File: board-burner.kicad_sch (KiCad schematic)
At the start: 44 parts, among them J1 Conn_01x04_Socket, J2 TH1, J3 FAN, J4 HEATER, J5 AUX2, J6 Micro_SD_Card, J7 AUX1, J8 TH2, J9 MAINS, Q1 2N7000, Q2 Q_NMOS_DGS, Q3 Q_PMOS_DGS, Q4 Q_NMOS_DGS, Q5 Q_NMOS_DGS, Q6 Q_NMOS_DGS, SW1 PWR, U1 10A SSR, U2 MAX31855KASA, U4 MAX31855KASA

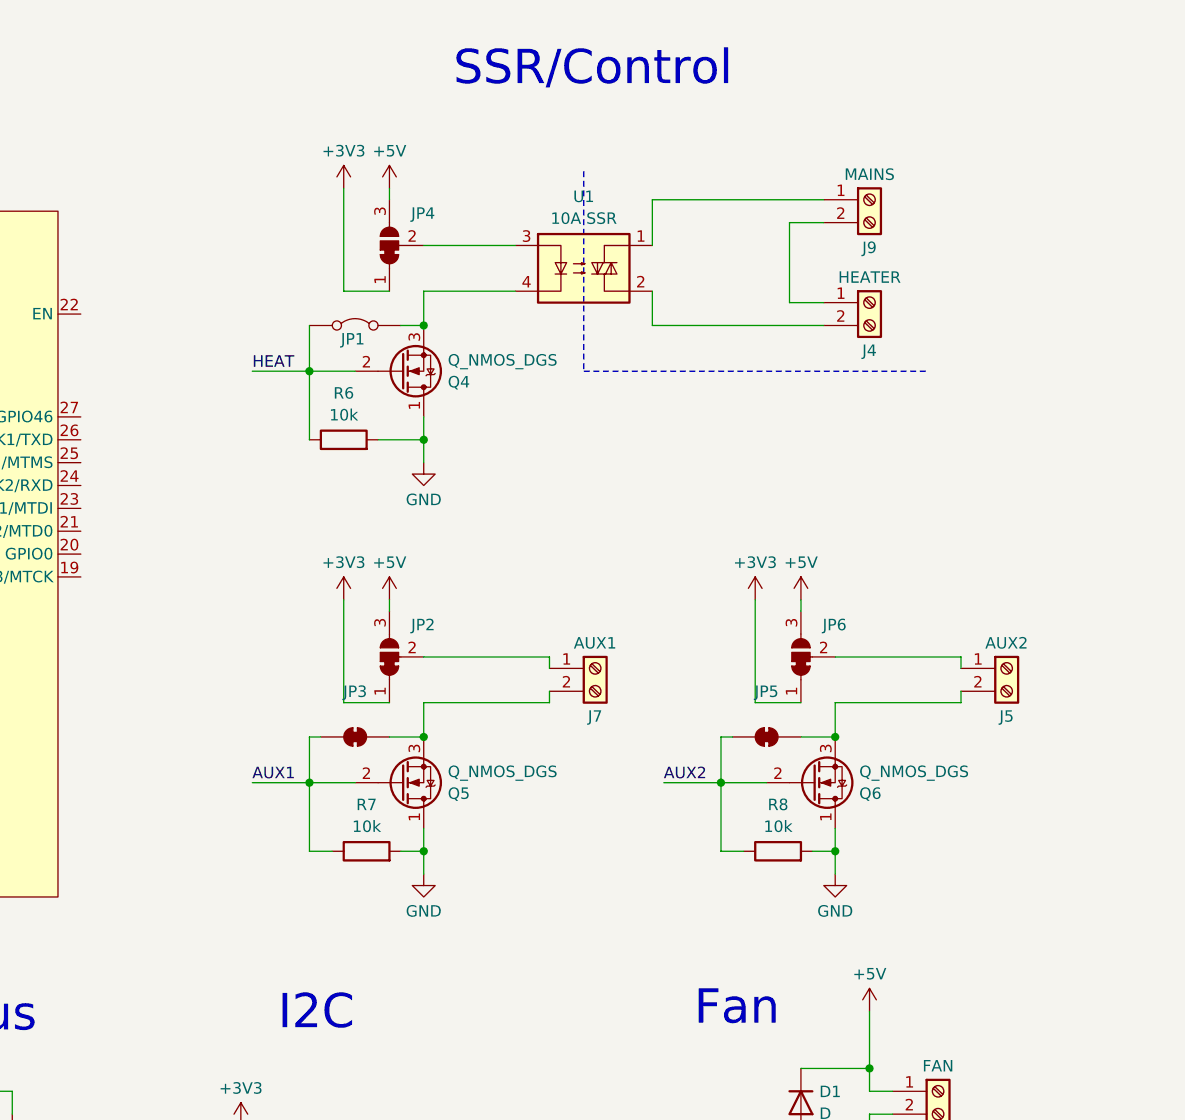
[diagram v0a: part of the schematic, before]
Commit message: Refactored SSRs into a hierarchical sheet
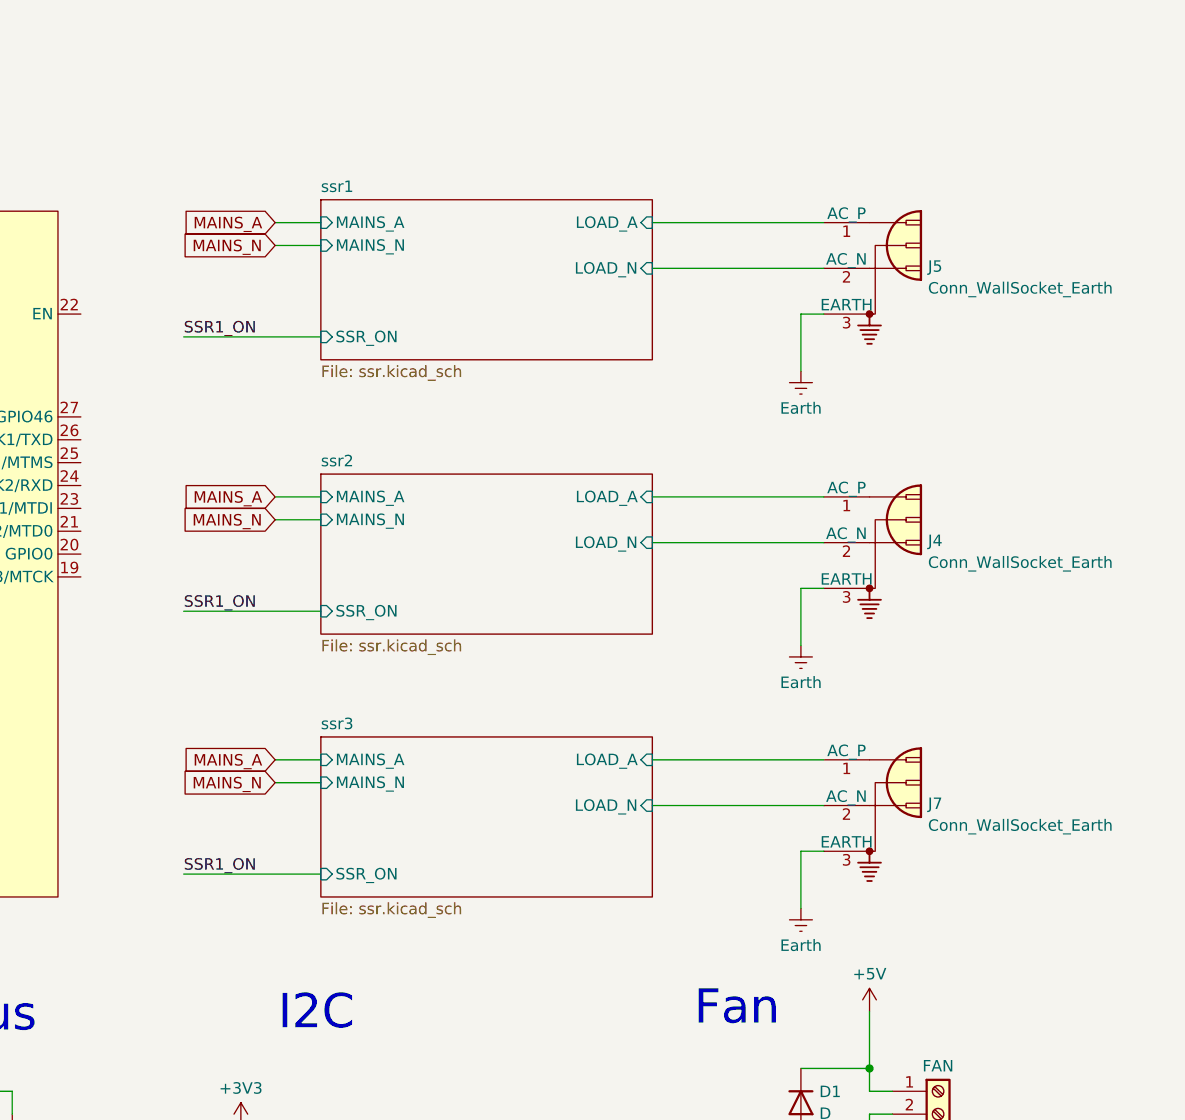
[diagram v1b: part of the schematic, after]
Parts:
- removed J4: HEATER, symbol Connector:Screw_Terminal_01x02
- removed J5: AUX2, symbol Connector:Screw_Terminal_01x02
- removed J7: AUX1, symbol Connector:Screw_Terminal_01x02
- removed J9: MAINS, symbol Connector:Screw_Terminal_01x02
- removed JP1: Jumper_2_Bridged, symbol Jumper:Jumper_2_Bridged
- removed JP2, JP4, JP6: SolderJumper_3_Bridged12, symbol Jumper:SolderJumper_3_Bridged12
- removed JP3, JP5: SolderJumper_2_Bridged, symbol Jumper:SolderJumper_2_Bridged
- removed Q4, Q5, Q6: Q_NMOS_DGS, symbol Device:Q_NMOS_DGS
- removed R6, R7, R8: 10k, symbol Device:R
- removed U1: 10A SSR, Package_SIP:SIP4_Sharp-SSR_P7.62mm_Straight, symbol Relay_SolidState:S202S01
- added J4, J5, J7: Conn_WallSocket_Earth, symbol Connector:Conn_WallSocket_Earth
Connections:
- new net Earth: J4.3 (EARTH), J5.3 (EARTH), J7.3 (EARTH)
- new net ssr1/LOAD_A: J5.1 (AC_P)
- new net ssr1/LOAD_N: J5.2 (AC_N)
- new net ssr2/LOAD_A: J4.1 (AC_P)
- new net ssr2/LOAD_N: J4.2 (AC_N)
- new net ssr3/LOAD_A: J7.1 (AC_P)
- new net ssr3/LOAD_N: J7.2 (AC_N)
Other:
- added sheet ssr1 (ssr.kicad_sch)
- added sheet ssr2 (ssr.kicad_sch)
- added sheet ssr3 (ssr.kicad_sch)
- note removed: "SSR/Control"

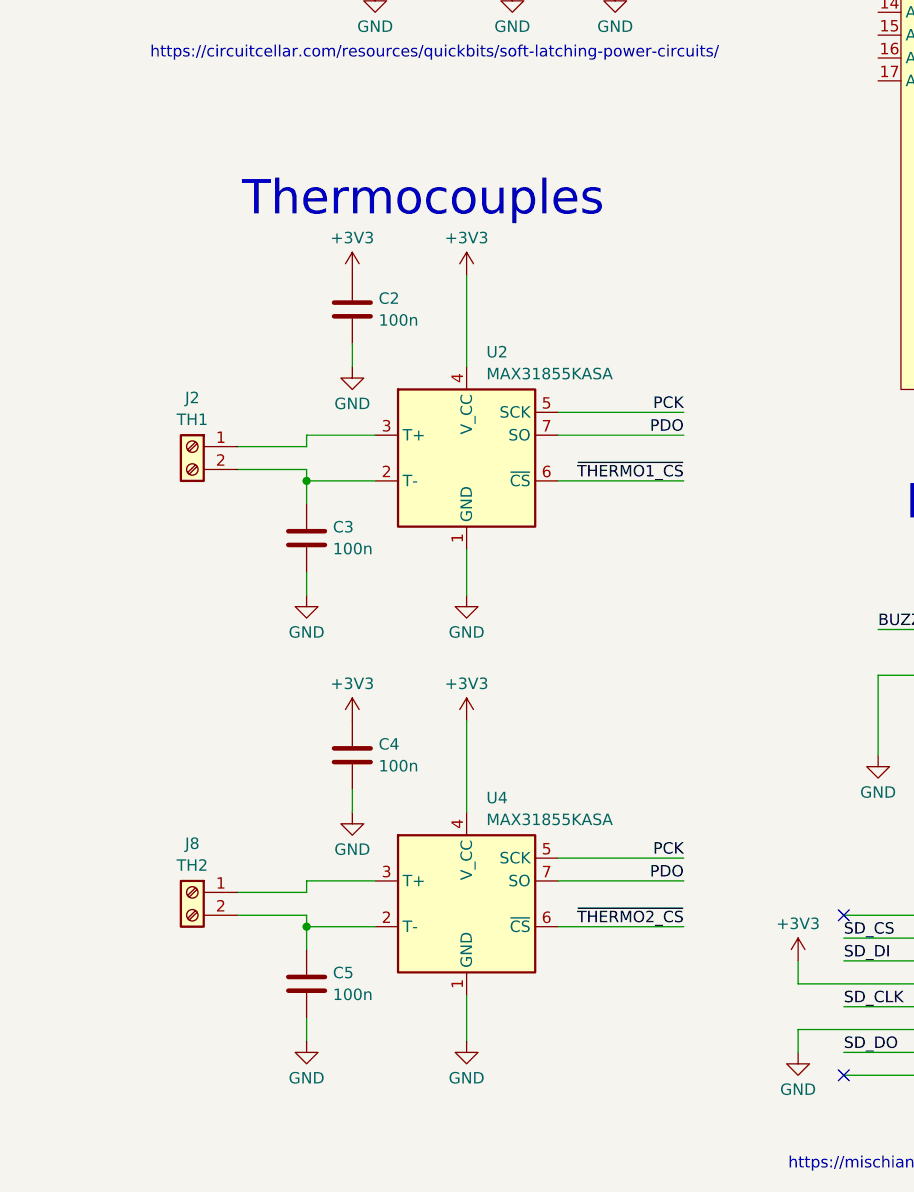
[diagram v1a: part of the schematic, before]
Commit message: Moved thermocouple chip into hierarchical sheet
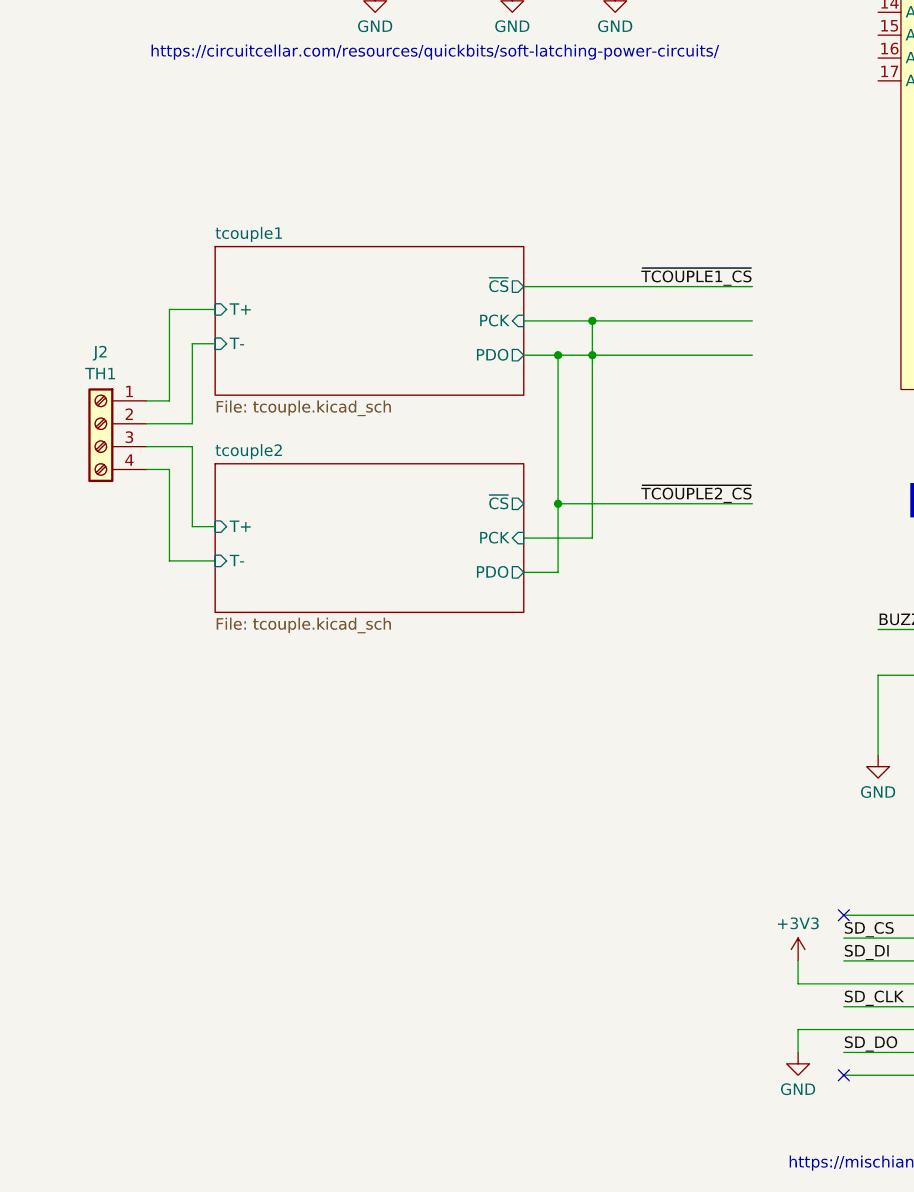
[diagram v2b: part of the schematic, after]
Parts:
- removed C2, C3, C4, C5: 100n, symbol Device:C
- removed J2: TH1, symbol Connector:Screw_Terminal_01x02
- removed J8: TH2, symbol Connector:Screw_Terminal_01x02
- removed U2, U4: MAX31855KASA, Package_SO:SOIC-8_3.9x4.9mm_P1.27mm, symbol Sensor_Temperature:MAX31855KASA
- added J2: TH1, symbol Connector:Screw_Terminal_01x04
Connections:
- new net tcouple1/T+: J2.1 (Pin_1)
- new net tcouple1/T-: J2.2 (Pin_2)
- new net tcouple2/T+: J2.3 (Pin_3)
- new net tcouple2/T-: J2.4 (Pin_4)
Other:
- added sheet tcouple1 (tcouple.kicad_sch)
- added sheet tcouple2 (tcouple.kicad_sch)
- note removed: "Thermocouples"

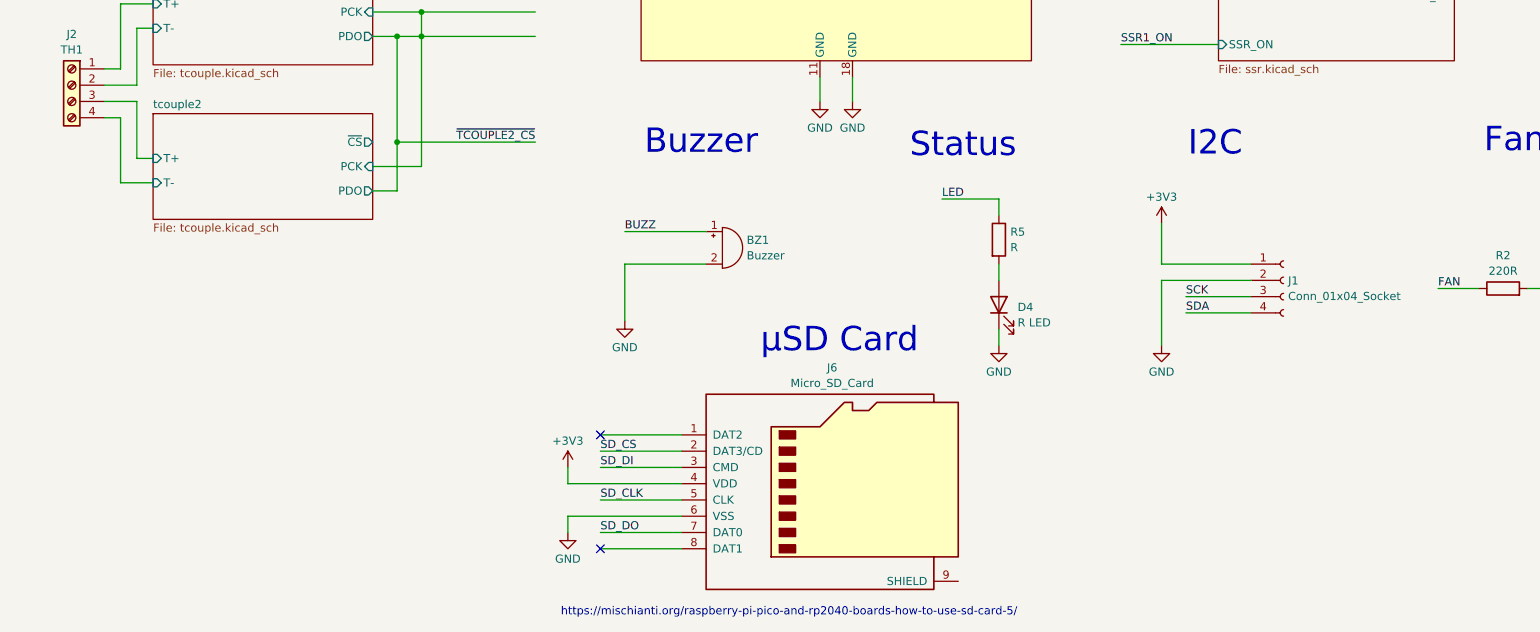
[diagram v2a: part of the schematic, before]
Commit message: Moved various parts to peripherals hierarchical sheet
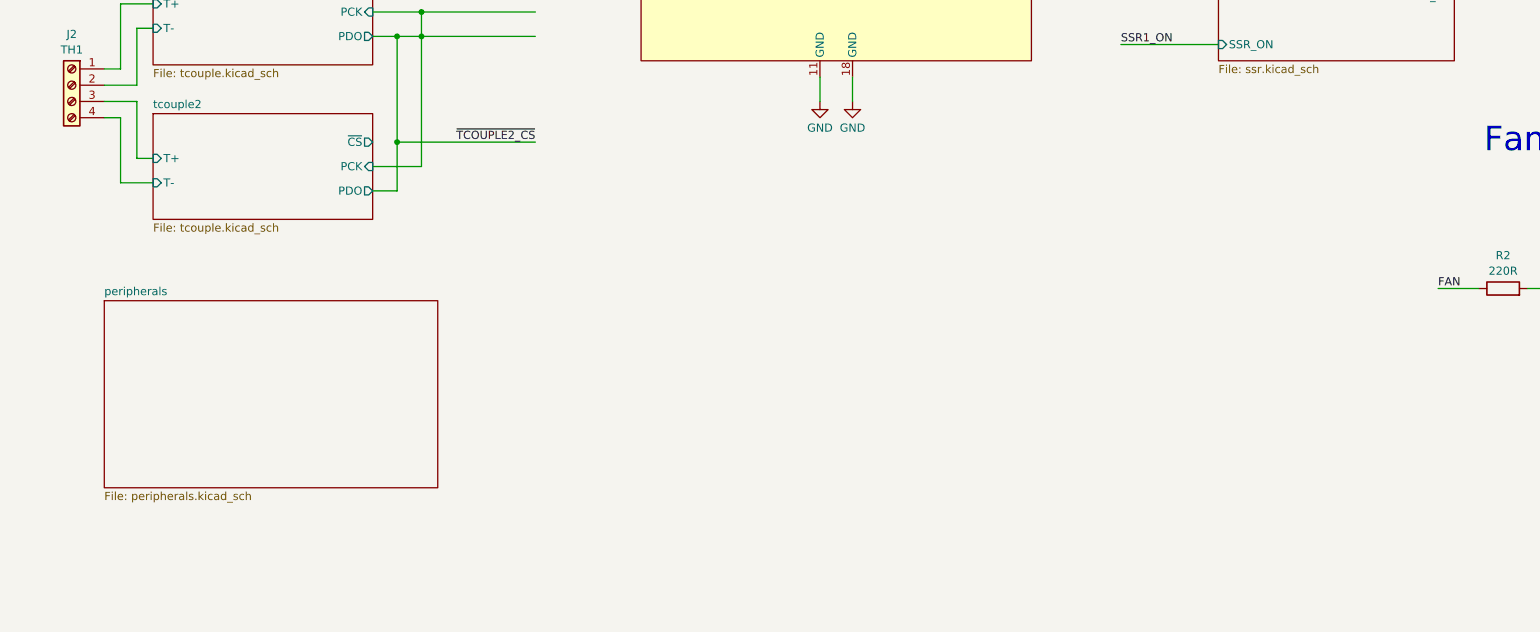
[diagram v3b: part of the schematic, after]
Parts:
- removed BZ1: Buzzer, symbol Device:Buzzer
- removed D4: R LED, symbol Device:LED
- removed J1: Conn_01x04_Socket, symbol Connector:Conn_01x04_Socket
- removed J6: Micro_SD_Card, symbol Connector:Micro_SD_Card
- removed R5: R, symbol Device:R
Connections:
- no-connect marks 2 -> 0
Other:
- added sheet peripherals (peripherals.kicad_sch)
- note removed: "Buzzer"
- note removed: "I2C"
- note removed: "Status"
- note removed: "https://mischianti.org/raspberry-pi-pico-and-rp2040-boards-how-to-use-sd-card-5/"
- note removed: "μSD Card"
